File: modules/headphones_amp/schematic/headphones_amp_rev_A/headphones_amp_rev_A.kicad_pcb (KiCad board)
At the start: 2 copper layers, 106 parts, among them J1 AudioJack3_SwitchTR, J2 AudioJack3_SwitchTR, J3 Conn_01x02, J4 Conn_01x02, Q1 BC140, Q10 BC548, Q11 BC548, Q12 BC140, Q13 BC160, Q14 BC548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

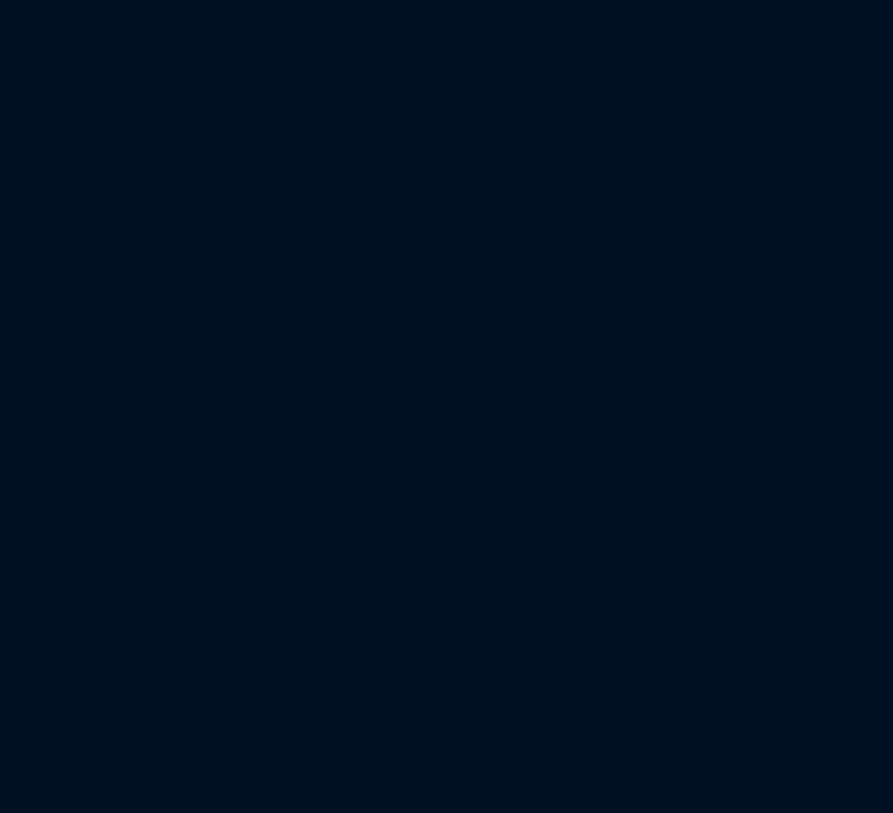
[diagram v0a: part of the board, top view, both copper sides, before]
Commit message: added footprint for the 5.08mm board connector
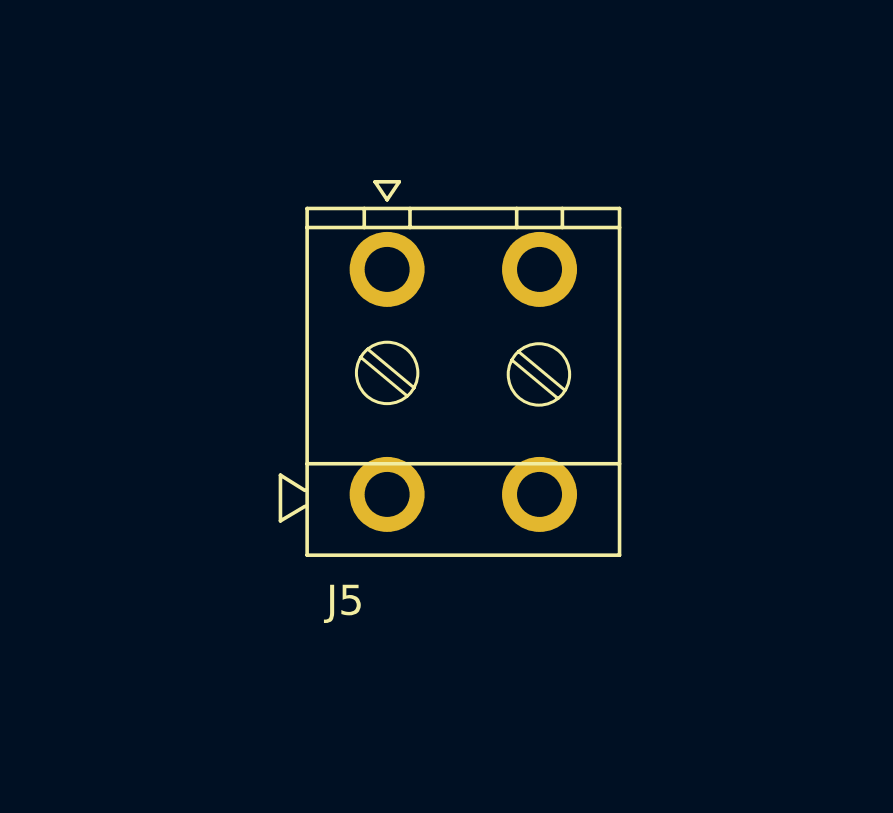
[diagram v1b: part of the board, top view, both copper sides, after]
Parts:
- added J5: Conn_01x02, ProjectLib_Transient:WuerthElectronik_WR_TBL_Series_2545_1x02_P5.08mm_Horizontal, F.Cu at (234.9, 25.0)
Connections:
- SW1 pad 1: unconnected-(SW1-Pad1) -> Net-(J5-Pin_2)

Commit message: added outline for the PCB
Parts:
- added RV8: 1k, ProjectLib_Transient:Potentiometer_Bourns_PTV09A-4_Single_Vertical, F.Cu at (381.0, 74.9)
- moved J3 344.1 mm to (382.5, 35.0)
- moved J4 344.1 mm to (380.0, 58.0)
- moved SW1 338.3 mm to (367.0, 49.7), turned to 90 degrees
- moved D1 304.1 mm to (365.5, 57.0)
- moved H2 282.2 mm to (434.0, 31.0)
- moved H3 280.4 mm to (434.0, 84.0)
- moved RV3 271.7 mm to (408.0, 68.0)
- moved H1 213.7 mm to (366.0, 31.0)
- moved H4 212.2 mm to (366.0, 84.0)
- moved J5 183.7 mm to (418.6, 28.4)
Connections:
- R21 pad 2: unconnected-(R21-Pad2) -> Net-(RV8-A)
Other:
- board outline added: 80 x 65 mm

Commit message: updated the pcb outline
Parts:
- moved C3 266.9 mm to (392.0, 50.0)
- moved J1 249.2 mm to (431.3, 46.6)
- moved Q8 229.1 mm to (415.4, 36.5), turned to 90 degrees
- moved C10 215.0 mm to (378.0, 49.0)
- moved R20 210.7 mm to (399.8, 31.0)
- moved R21 210.7 mm to (399.8, 35.0)
- moved R22 210.7 mm to (399.8, 39.1)
- moved R23 210.7 mm to (399.8, 43.1)
- moved J2 210.4 mm to (447.0, 72.0), turned to 180 degrees
- moved C9 205.8 mm to (378.0, 64.0)
- moved SW2 178.7 mm to (365.0, 87.7), turned to 90 degrees
- moved RV3 49.6 mm to (383.2, 111.0), turned to 90 degrees
- moved J4 40.4 mm to (365.0, 95.5), turned to 90 degrees
- moved J5 40.0 mm to (378.6, 28.4)
- moved J3 36.5 mm to (365.0, 67.0), turned to 90 degrees
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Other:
- board size 80 x 65 mm -> 90 x 90 mm

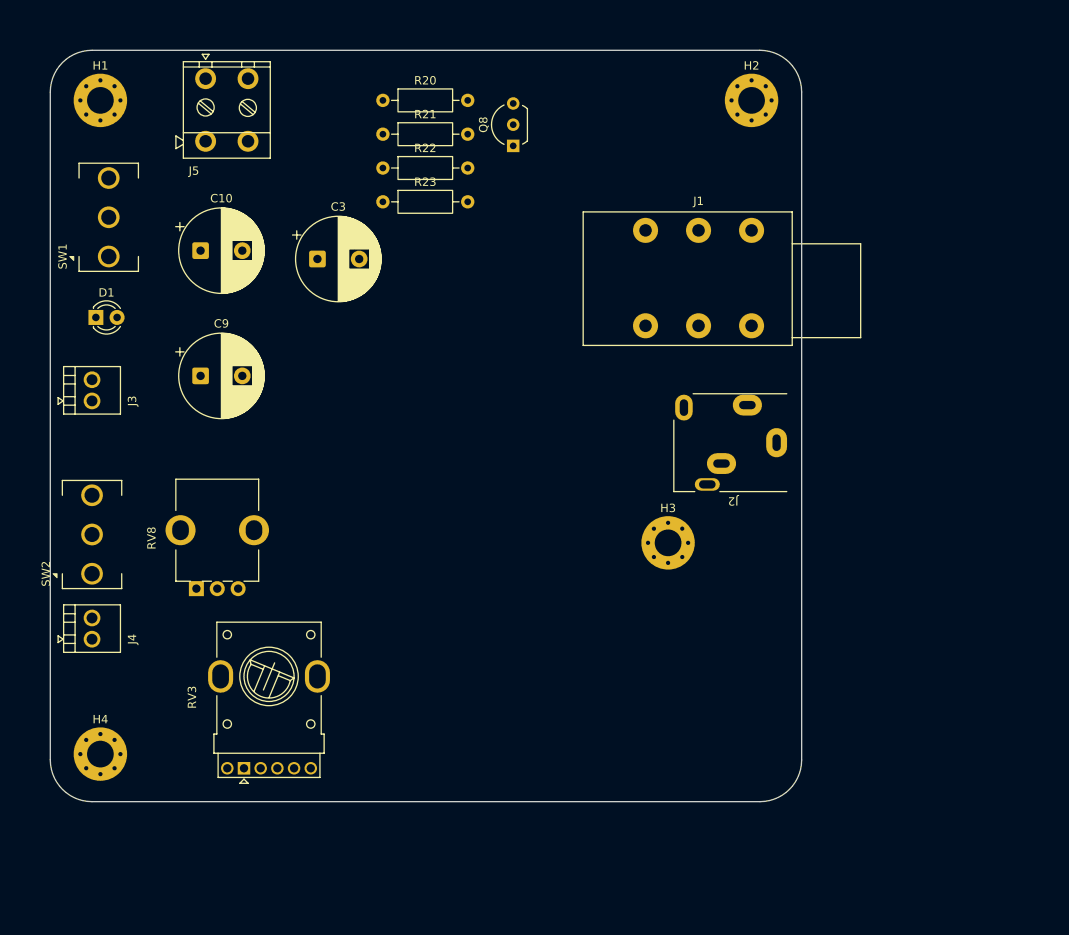
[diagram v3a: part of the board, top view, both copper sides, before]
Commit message: extended PCB outline
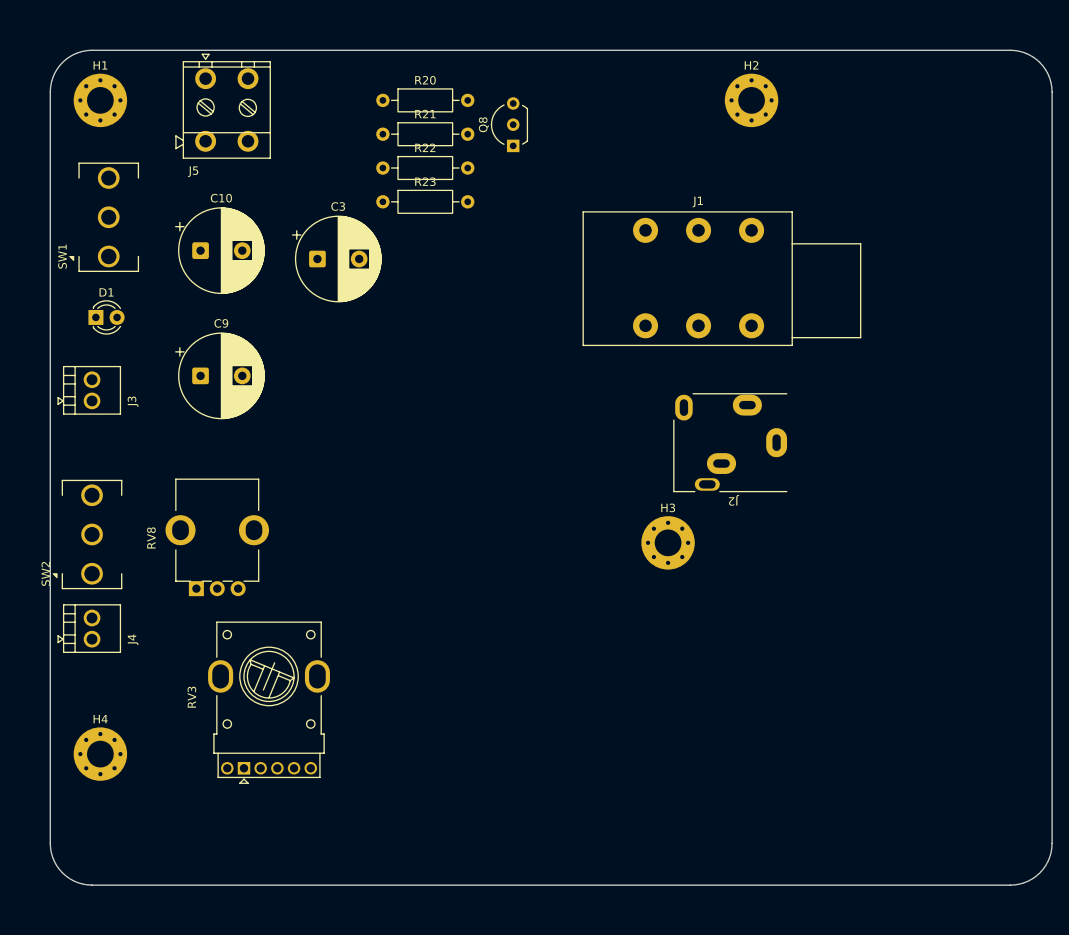
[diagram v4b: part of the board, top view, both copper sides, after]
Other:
- board size 90 x 90 mm -> 120 x 100 mm
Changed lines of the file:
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@@
 	(gr_line
 		(start 360 30)
-		(end 360 110)
+		(end 360 120)
+		(stroke
+			(width 0.05)
+			(type default)
+		)
+		(layer "Edge.Cuts")
+	)
+	(gr_arc
+		(start 365 125)
+		(mid 361.464466 123.535534)
+		(end 360 120)
 		(stroke
 			(width 0.05)
@@
 	)
 	(gr_arc
-		(start 445 25)
-		(mid 448.535534 26.464466)
-		(end 450 30)
+		(start 475 25)
+		(mid 478.535534 26.464466)
+		(end 480 30)
 		(stroke
 			(width 0.05)
@@
 	(gr_line
 		(start 365 25)
-		(end 445 25)
+		(end 475 25)
 		(stroke
 			(width 0.05)
@@
 	)
 	(gr_line
-		(start 365 115)
-		(end 445 115)
+		(start 365 125)
+		(end 475 125)
 		(stroke
 			(width 0.05)
@@
 	)
 	(gr_arc
-		(start 450 110)
-		(mid 448.535534 113.535534)
-		(end 445 115)
-		(stroke
-			(width 0.05)
-			(type default)
-		)
-		(layer "Edge.Cuts")
-	)
-	(gr_arc
-		(start 365 115)
-		(mid 361.464466 113.535534)
-		(end 360 110)
+		(start 480 120)
+		(mid 478.535534 123.535534)
+		(end 475 125)
 		(stroke
 			(width 0.05)
@@
 	)
 	(gr_line
-		(start 450 30)
-		(end 450 110)
+		(start 480 30)
+		(end 480 120)
 		(stroke
 			(width 0.05)

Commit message: adjusted bias point of the input stage first preplacement of the parts on the board
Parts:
- moved Q8 347.0 mm to (82.0, 132.5)
- moved H4 326.7 mm to (48.0, 184.0)
- moved C10 324.6 mm to (60.0, 114.0)
- moved C3 324.6 mm to (74.0, 115.0)
- moved C9 324.6 mm to (60.0, 129.0)
- moved D1 324.6 mm to (47.5, 122.0)
- moved H1 324.6 mm to (48.0, 96.0)
- moved J3 324.6 mm to (47.0, 132.0)
- moved J4 324.6 mm to (47.0, 160.5)
- moved J5 324.6 mm to (60.6, 93.4)
- moved R20 324.6 mm to (81.8, 96.0)
- moved R21 324.6 mm to (81.8, 100.0)
- moved R22 324.6 mm to (81.8, 104.1)
- moved R23 324.6 mm to (81.8, 108.2)
- moved RV3 324.6 mm to (65.2, 176.0)
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
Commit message: updated the article
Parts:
- added J6: Conn_01x02, ProjectLib_Transient:WuerthElectronik_WR_TBL_Series_2109_1x02_P2.54mm_Horizontal, F.Cu at (147.8, 153.0)
- added J7: Conn_01x02, ProjectLib_Transient:WuerthElectronik_WR_TBL_Series_2109_1x02_P2.54mm_Horizontal, F.Cu at (155.5, 153.0)
- moved R41 156.4 mm to (114.8, 170.0)
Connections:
- J1 pad RN: unconnected-(J1-PadRN) -> Net-(J1-PadRN)
- J1 pad TN: unconnected-(J1-PadTN) -> Net-(J1-PadTN)
- J2 pad R: unconnected-(J2-PadR) -> Net-(J1-PadRN)
- J2 pad S: unconnected-(J2-PadS) -> GND
- J2 pad T: unconnected-(J2-PadT) -> Net-(J1-PadTN)

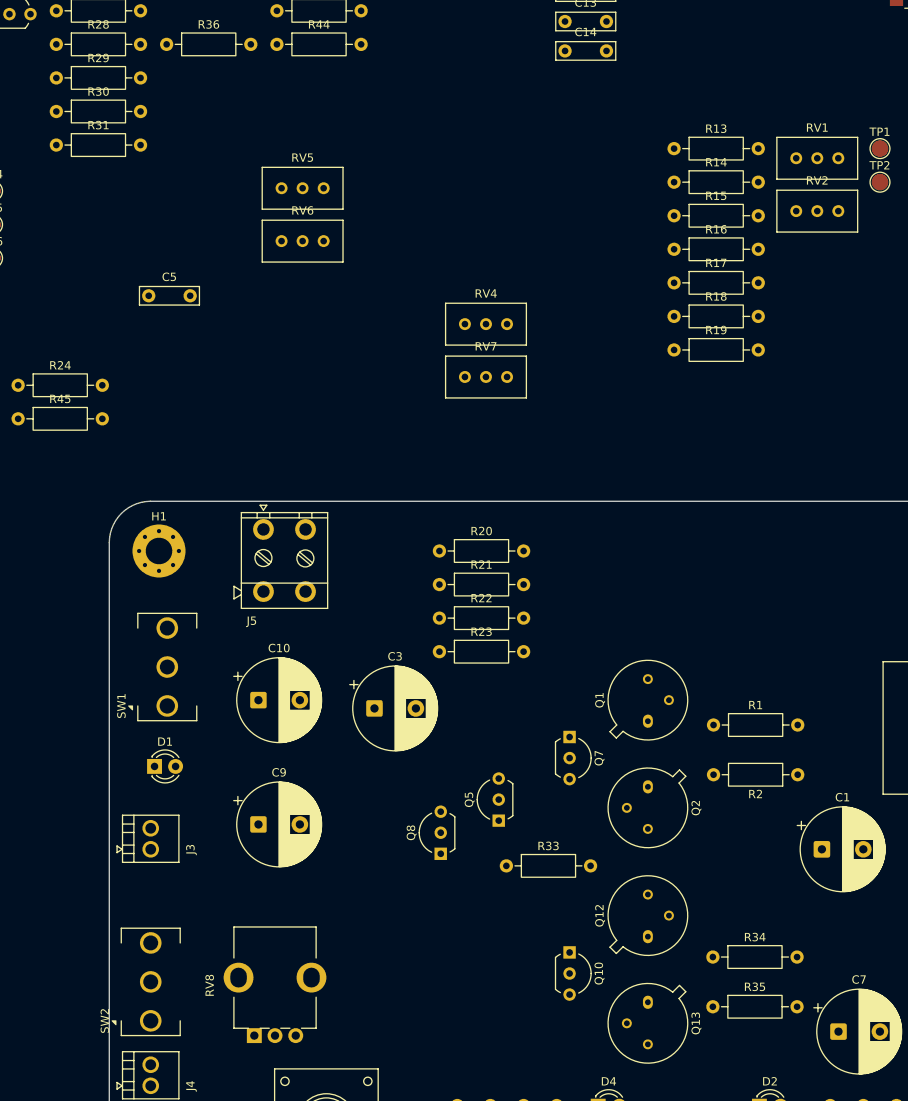
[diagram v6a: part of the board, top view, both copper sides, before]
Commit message: updated rubber diode section
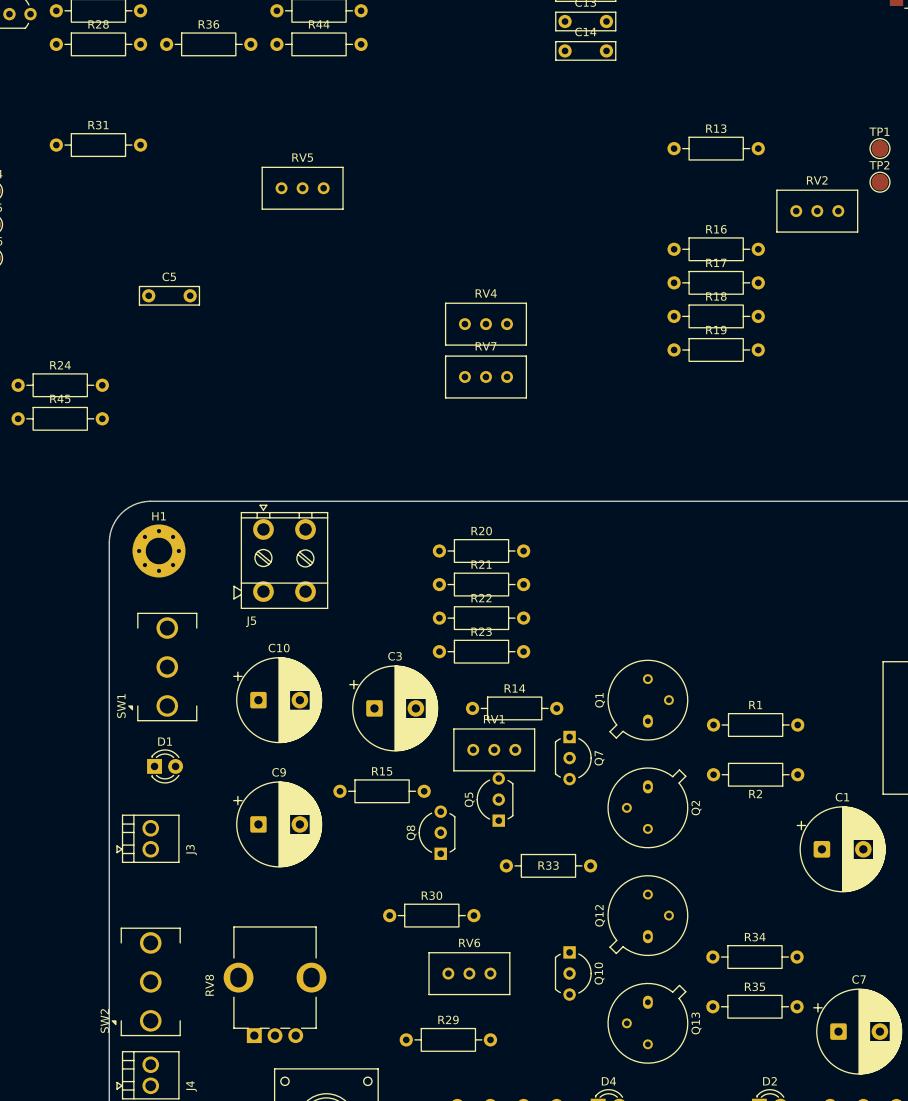
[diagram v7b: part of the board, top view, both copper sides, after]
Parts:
- moved R29 123.5 mm to (77.8, 155.0)
- moved R30 105.0 mm to (75.8, 140.0)
- moved RV6 90.7 mm to (88.0, 147.0)
- moved RV1 81.3 mm to (91.0, 120.0)
- moved R15 80.3 mm to (69.8, 125.0)
- moved R14 68.0 mm to (85.8, 115.0)
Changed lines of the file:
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@@
 		(tags "Resistor Axial_DIN0207 series Axial Horizontal pin pitch 10.16mm 0.25W = 1/4W length 6.3mm diameter 2.5mm")
 		(property "Reference" "R33"
-			(at 5.08 -2.37 0)
+			(at 5.08 0 0)
 			(layer "F.SilkS")
 			(effects
@@
 			(layer "F.Fab")
 		)
-		(fp_text user "${REFERENCE}"
-			(at 5.08 0 0)
-			(layer "F.Fab")
-			(effects
-				(font
-					(size 1 1)
-					(thickness 0.15)
-				)
-			)
-		)
 		(pad "1" thru_hole circle
 			(at 0 0)
@@
 			(at 2.54 2.79 90)
 			(layer "F.Fab")
+			(hide yes)
 			(effects
 				(font
@@
 	(footprint "Resistor_THT:R_Axial_DIN0207_L6.3mm_D2.5mm_P10.16mm_Horizontal"
 		(layer "F.Cu")
-		(at 110.16 55.54)
+		(at 69.84 125)
 		(descr "Resistor, Axial_DIN0207 series, Axial, Horizontal, pin pitch=10.16mm, 0.25W = 1/4W, length*diameter=6.3*2.5mm^2, http://cdn-reichelt.de/documents/datenblatt/B400/1_4W%23YAG.pdf")
 		(tags "Resistor Axial_DIN0207 series Axial Horizontal pin pitch 10.16mm 0.25W = 1/4W length 6.3mm diameter 2.5mm")
@@
 	(footprint "Potentiometer_THT:Potentiometer_Bourns_3296W_Vertical"
 		(layer "F.Cu")
-		(at 129.98 48.6)
+		(at 91 120)
 		(descr "Potentiometer, vertical, Bourns 3296W, https://www.bourns.com/pdfs/3296.pdf")
 		(tags "Potentiometer vertical Bourns 3296W")
@@
 	(footprint "Resistor_THT:R_Axial_DIN0207_L6.3mm_D2.5mm_P10.16mm_Horizontal"
 		(layer "F.Cu")
-		(at 110.16 51.49)
+		(at 85.84 115)
 		(descr "Resistor, Axial_DIN0207 series, Axial, Horizontal, pin pitch=10.16mm, 0.25W = 1/4W, length*diameter=6.3*2.5mm^2, http://cdn-reichelt.de/documents/datenblatt/B400/1_4W%23YAG.pdf")
 		(tags "Resistor Axial_DIN0207 series Axial Horizontal pin pitch 10.16mm 0.25W = 1/4W length 6.3mm diameter 2.5mm")
@@
 	(footprint "Resistor_THT:R_Axial_DIN0207_L6.3mm_D2.5mm_P10.16mm_Horizontal"
 		(layer "F.Cu")
-		(at 35.61 38.91)
+		(at 77.84 155)
 		(descr "Resistor, Axial_DIN0207 series, Axial, Horizontal, pin pitch=10.16mm, 0.25W = 1/4W, length*diameter=6.3*2.5mm^2, http://cdn-reichelt.de/documents/datenblatt/B400/1_4W%23YAG.pdf")
 		(tags "Resistor Axial_DIN0207 series Axial Horizontal pin pitch 10.16mm 0.25W = 1/4W length 6.3mm diameter 2.5mm")
@@
 	(footprint "Resistor_THT:R_Axial_DIN0207_L6.3mm_D2.5mm_P10.16mm_Horizontal"
 		(layer "F.Cu")
-		(at 35.61 42.96)
+		(at 75.84 140)
 		(descr "Resistor, Axial_DIN0207 series, Axial, Horizontal, pin pitch=10.16mm, 0.25W = 1/4W, length*diameter=6.3*2.5mm^2, http://cdn-reichelt.de/documents/datenblatt/B400/1_4W%23YAG.pdf")
 		(tags "Resistor Axial_DIN0207 series Axial Horizontal pin pitch 10.16mm 0.25W = 1/4W length 6.3mm diameter 2.5mm")
@@
 	(footprint "Potentiometer_THT:Potentiometer_Bourns_3296W_Vertical"
 		(layer "F.Cu")
-		(at 67.87 58.6)
+		(at 88 147)
 		(descr "Potentiometer, vertical, Bourns 3296W, https://www.bourns.com/pdfs/3296.pdf")
 		(tags "Potentiometer vertical Bourns 3296W")
@@
 			(at 2.54 2.79 90)
 			(layer "F.Fab")
+			(hide yes)
 			(effects
 				(font
